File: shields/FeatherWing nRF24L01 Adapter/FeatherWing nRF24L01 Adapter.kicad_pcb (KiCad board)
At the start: 2 copper layers, 50.9 x 22.9 mm, 15 parts, among them SW1 SWITCH_TACT_SMT4.6X2.8, U1 nRF24L01

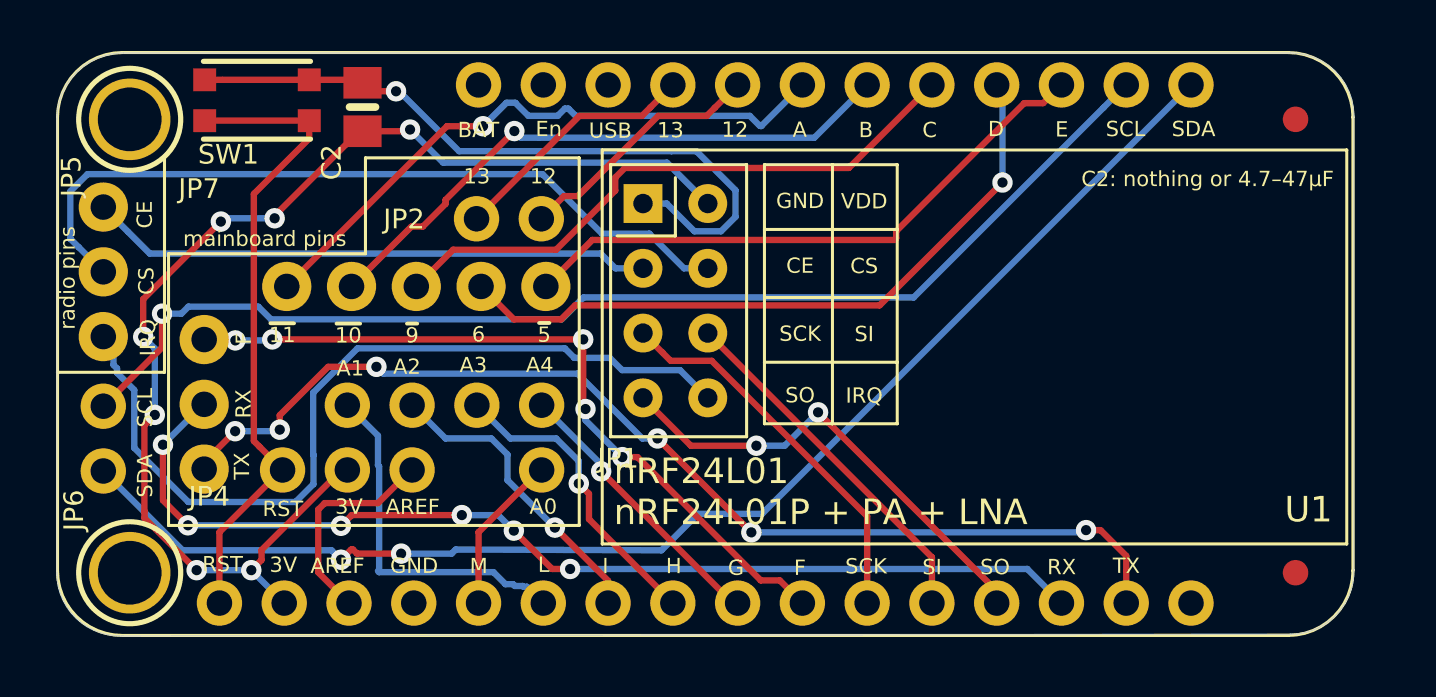
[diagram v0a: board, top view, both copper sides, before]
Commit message: changed nRF24 module to E01-ML01SP2
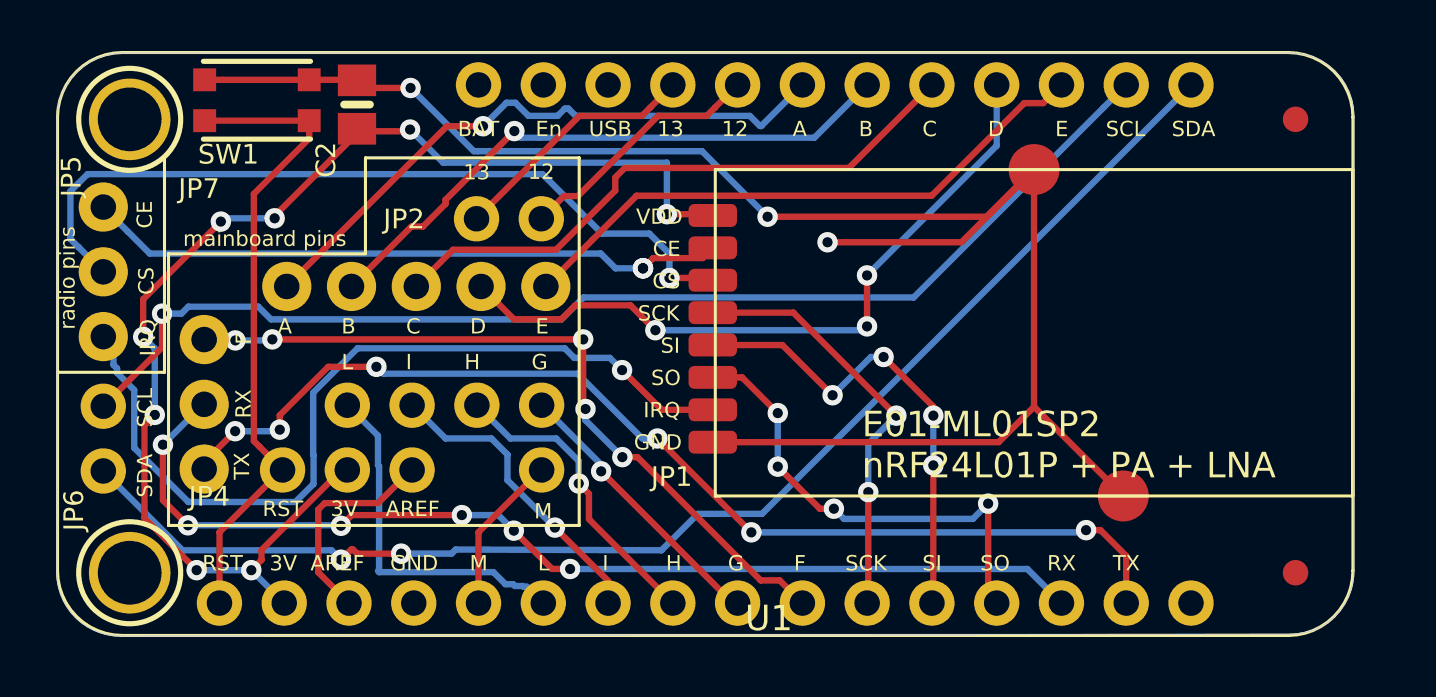
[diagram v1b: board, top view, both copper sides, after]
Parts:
- U1: value nRF24L01 -> nRF24L01_PA_LNA_E01_ML01SP2; footprint FeatherWing nRF24L01 Adapter:nRF24L01_Breakout -> FeatherWing nRF24L01 Adapter:E01-ML01SP2
- moved U1 18.2 mm to (132.2, 99.8)
- moved C2 0.24 mm to (111.2, 80.7)
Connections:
- U1 pad 1: GND -> 3.3V
- U1 pad 2: 3.3V -> /CE
- U1 pad 3: /CE -> /CS
- U1 pad 4: /CS -> /SCK
- U1 pad 5: /SCK -> /MOSI
- U1 pad 6: /MOSI -> /MISO
- U1 pad 7: /MISO -> /IRQ
- U1 pad 8: /IRQ -> GND
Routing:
- net GND: track 28.0 -> 72.2 mm, vias 1 -> 3
- net /MOSI: track 14.2 -> 18.6 mm, vias 0 -> 4
- net /CE: track 22.2 -> 25.2 mm, vias 0 -> 2
- net 3.3V: track 47.5 -> 49.1 mm, vias 7 -> 8
- net /SCK: track 15.2 -> 16.7 mm, vias 0 -> 2
- net /D: track 27.1 -> 28.3 mm, vias 1 -> 3
- net /CS: track 30.5 -> 31.4 mm, vias 0 -> 1
- net /MISO: track 18.6 -> 19.1 mm, vias 2 -> 4
- net /IRQ: track 33.6 -> 34.0 mm, vias 0 -> 1
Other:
- board text added: "E01-ML01SP2 nRF24L01P + PA + LNA"
- board text removed: "6"
- board text removed: "A0"
- board text removed: "A1"
- board text removed: "A2"
- board text removed: "A3"
- board text removed: "A4"
- board text removed: "C2: nothing or 4.7–47µF"
- board text removed: "nRF24L01 nRF24L01P + PA + LNA"
- board text removed: "~10"
- board text removed: "~11"
- board text removed: "~5"
- board text removed: "~9"

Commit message: Added E01-ML01SP2 module shield
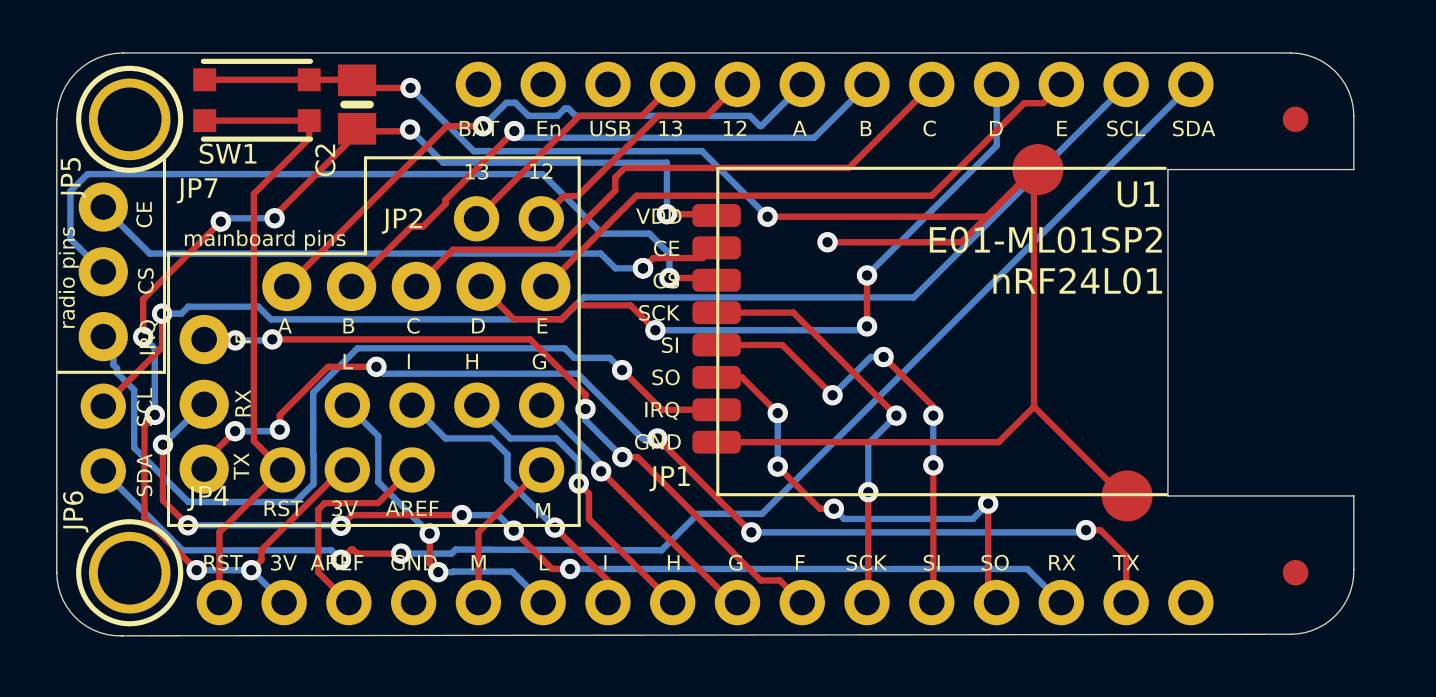
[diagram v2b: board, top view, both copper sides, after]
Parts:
- removed U$16: , FeatherWing nRF24L01 Adapter:FEATHERLOGO
- moved U1 0.15 mm to (132.3, 99.8)
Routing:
- net /L: track 14.1 -> 12.6 mm, vias 0 -> 2
- net /F: track 29.6 -> 28.5 mm, vias 5 -> 4
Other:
- outline, holes or cut-outs redrawn
- board text added: "E01-ML01SP2 nRF24L01"
- board text added: "nRF24L01 FeatherWing https://twitter.com/RFQuack"
- board text removed: "E01-ML01SP2 nRF24L01P + PA + LNA"
- board text removed: "twitter.com/rfquack"
